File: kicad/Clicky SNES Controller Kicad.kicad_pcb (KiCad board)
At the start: 2 copper layers, 70.2 x 44.8 mm, 0 parts

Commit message: Set up OSH Park design rules
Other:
- net class Default: clearance 0.2 -> 0.1524; trace_width 0.25 -> 0.1524; via_dia 0.6 -> 0.6858; via_drill 0.4 -> 0.3302
- rule trace_clearance: 0.2 -> 0.1524
- rule trace_min: 0.2 -> 0.1524
- rule via_min_drill: 0.3 -> 0.3302
- rule via_min_size: 0.4 -> 0.6858
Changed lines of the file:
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@@
     (links 0)
     (no_connects 0)
-    (area 13.71421 14.16482 172.72886 59.104601)
-    (thickness 1.6)
+    (area 13.71421 14.16482 181.453135 62.567801)
+    (thickness 1.6002)
     (drawings 175)
     (tracks 0)
@@
     (0 F.Cu signal)
     (31 B.Cu signal)
-    (32 B.Adhes user)
-    (33 F.Adhes user)
-    (34 B.Paste user)
-    (35 F.Paste user)
+    (32 B.Adhes user hide)
+    (33 F.Adhes user hide)
+    (34 B.Paste user hide)
+    (35 F.Paste user hide)
     (36 B.SilkS user)
     (37 F.SilkS user)
@@
     (40 Dwgs.User user)
     (41 Cmts.User user)
-    (42 Eco1.User user)
-    (43 Eco2.User user)
+    (42 Eco1.User user hide)
+    (43 Eco2.User user hide)
     (44 Edge.Cuts user)
-    (45 Margin user)
-    (46 B.CrtYd user)
-    (47 F.CrtYd user)
-    (48 B.Fab user)
-    (49 F.Fab user)
+    (45 Margin user hide)
+    (46 B.CrtYd user hide)
+    (47 F.CrtYd user hide)
+    (48 B.Fab user hide)
+    (49 F.Fab user hide)
   )
   (setup
-    (last_trace_width 0.25)
-    (trace_clearance 0.2)
+    (last_trace_width 0.1524)
+    (trace_clearance 0.1524)
     (zone_clearance 0.508)
     (zone_45_only no)
-    (trace_min 0.2)
+    (trace_min 0.1524)
     (segment_width 0.2)
     (edge_width 0.15)
-    (via_size 0.6)
-    (via_drill 0.4)
-    (via_min_size 0.4)
-    (via_min_drill 0.3)
-    (uvia_size 0.3)
-    (uvia_drill 0.1)
+    (via_size 0.6858)
+    (via_drill 0.3302)
+    (via_min_size 0.6858)
+    (via_min_drill 0.3302)
+    (uvia_size 0.762)
+    (uvia_drill 0.508)
     (uvias_allowed no)
-    (uvia_min_size 0.2)
-    (uvia_min_drill 0.1)
+    (uvia_min_size 0.762)
+    (uvia_min_drill 0.508)
     (pcb_text_width 0.3)
     (pcb_text_size 1.5 1.5)
@@
   (net 0 "")
   (net_class Default "This is the default net class."
-    (clearance 0.2)
-    (trace_width 0.25)
-    (via_dia 0.6)
-    (via_drill 0.4)
-    (uvia_dia 0.3)
-    (uvia_drill 0.1)
+    (clearance 0.1524)
+    (trace_width 0.1524)
+    (via_dia 0.6858)
+    (via_drill 0.3302)
+    (uvia_dia 0.762)
+    (uvia_drill 0.508)
   )
   (dimension 9.118742 (width 0.3) (layer Cmts.User)

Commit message: Restart PCB with OSH Park blank template
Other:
- board outline removed
- net class 0.2mm added: clearance 0.2, trace_width 0.2, via_dia 0.6858, via_drill 0.3302
- net class Default: clearance 0.1524 -> 0.254; trace_width 0.1524 -> 0.254
- net class Minimal added: clearance 0.1524, trace_width 0.1524, via_dia 0.6858, via_drill 0.3302
- rule pad_to_mask_clearance: 0.2 -> 0.05
- rule trace_clearance: 0.1524 -> 0.254

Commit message: PCB Rev 2: Create basic board outline
Re-imported the vector drawing of the mechanical board outline and put
the mirrored copy on a different layer so it can be differentiated by
color.
Eco1.User is the unmirrored drawing.
Eco2.User is the mirrored drawing

Added some mechanical keep-out areas to these layers as well.
I probably need two new layers for these but, for now, they are on the
same user layers.
The wide circles on Eco1.User are the keep-out areas behind the d-pad;
so these will actually collide with components placed on the back side
of the board.
The wide circles on Eco2.User are the keep-out areas behind the ABXY
buttons; so these will actually collide with components placed on the
front side of the board.

Created a board outline only for the main section.
I think I will need the extra room and have to use all 3 of these
for the main circuit board. The LR button boards can be done separately
if desired; but, for now, there isn't a good place to stick them
without increasing board rectangular size substantially.
Also OSH Park doesn't support V-grooves.
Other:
- board outline added: 41.9 x 44.8 mm

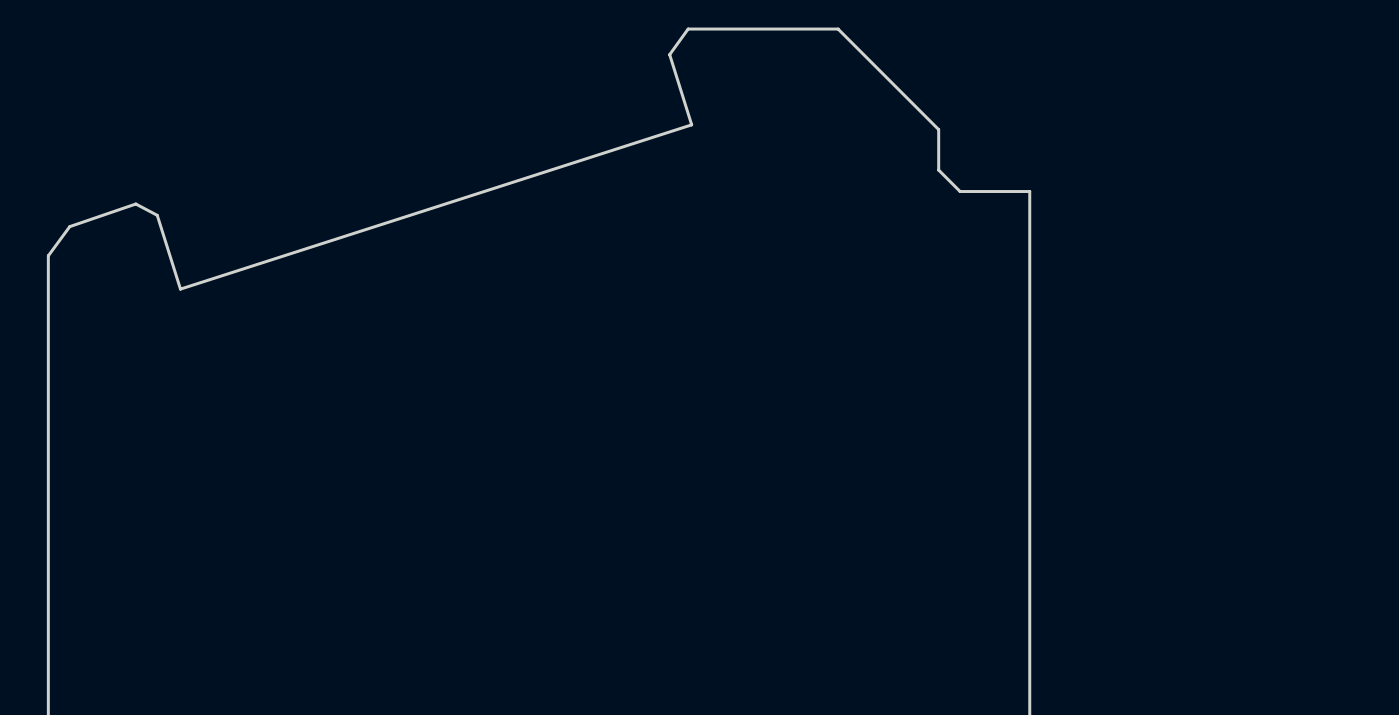
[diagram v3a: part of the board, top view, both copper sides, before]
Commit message: PCB Rev 2: Add mounting holes
Added some drill holes to the main board.
Still need to figure out the final position for the hole on the start /
select board, but a placeholder is in the file for now.
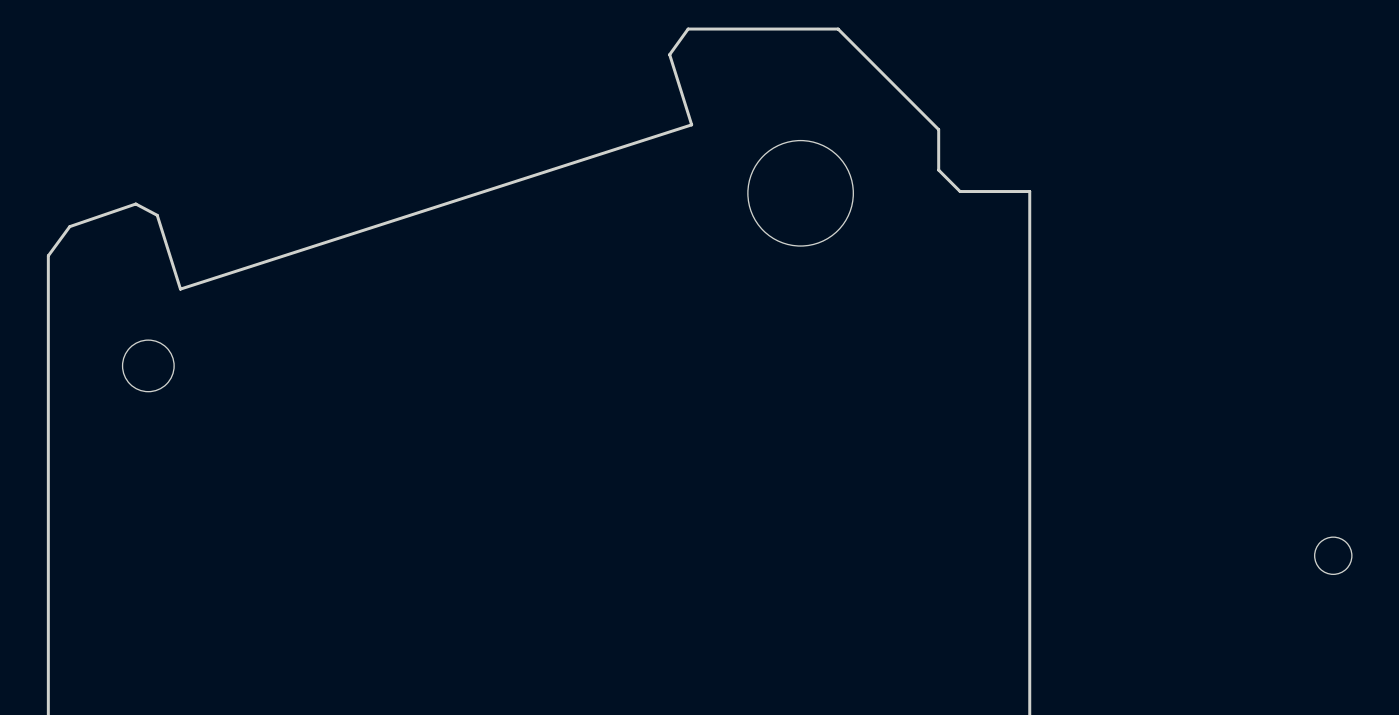
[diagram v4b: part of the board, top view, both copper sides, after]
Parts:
- added REF**: MountingHole_2.2mm_M2, Mounting_Holes:MountingHole_2.2mm_M2, F.Cu at (17.0, 27.4)
- added REF**: MountingHole_4.5mm, Mounting_Holes:MountingHole_4.5mm, F.Cu at (44.8, 20.0)
- added REF**: MountingHole_1_16th, Mounting_Holes:MountingHole_2.2mm_M2, F.Cu at (67.6, 35.5)
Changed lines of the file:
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@@
     (area 12.64741 12.76782 186.348413 57.779876)
     (thickness 1.6)
-    (drawings 174)
+    (drawings 177)
     (tracks 0)
     (zones 0)
-    (modules 0)
+    (modules 3)
     (nets 1)
   )
@@
     (mod_text_size 0.6 0.6)
     (mod_text_width 0.127)
-    (pad_size 1.524 1.524)
-    (pad_drill 0.762)
+    (pad_size 1.5875 1.5875)
+    (pad_drill 1.5875)
     (pad_to_mask_clearance 0.05)
     (pad_to_paste_clearance -0.04)
     (aux_axis_origin 0 0)
-    (visible_elements 7FFFFFFF)
+    (visible_elements 7FFFFF7F)
     (pcbplotparams
       (layerselection 0x3ffff_80000001)
@@
     (uvia_drill 0.127)
   )
+  (module Mounting_Holes:MountingHole_2.2mm_M2 (layer F.Cu)
+    (at 16.9926 27.3558)
+    (descr "Mounting Hole 2.2mm, no annular, M2")
+    (tags "mounting hole 2.2mm no annular m2")
+    (fp_text reference REF** (at 0 -3.2) (layer F.SilkS) hide
+      (effects (font (size 1 1) (thickness 0.15)))
+    )
+    (fp_text value MountingHole_2.2mm_M2 (at 0 3.2) (layer F.Fab) hide
+      (effects (font (size 1 1) (thickness 0.15)))
+    )
+    (fp_circle (center 0 0) (end 2.2 0) (layer Cmts.User) (width 0.15))
+    (fp_circle (center 0 0) (end 2.45 0) (layer F.CrtYd) (width 0.05))
+    (pad 1 np_thru_hole circle (at 0 0) (size 2.2 2.2) (drill 2.2) (layers *.Cu *.Mask))
+  )
+  (module Mounting_Holes:MountingHole_4.5mm (layer F.Cu)
+    (at 44.831 19.9898)
+    (descr "Mounting Hole 4.5mm, no annular")
+    (tags "mounting hole 4.5mm no annular")
+    (fp_text reference REF** (at 0 -5.5) (layer F.SilkS) hide
+      (effects (font (size 1 1) (thickness 0.15)))
+    )
+    (fp_text value MountingHole_4.5mm (at 0 5.5) (layer F.Fab) hide
+      (effects (font (size 1 1) (thickness 0.15)))
+    )
+    (fp_circle (center 0 0) (end 4.5 0) (layer Cmts.User) (width 0.15))
+    (fp_circle (center 0 0) (end 4.75 0) (layer F.CrtYd) (width 0.05))
+    (pad 1 np_thru_hole circle (at 0 0) (size 4.5 4.5) (drill 4.5) (layers *.Cu *.Mask))
+  )
+  (module Mounting_Holes:MountingHole_2.2mm_M2 (layer F.Cu)
+    (at 67.564 35.4584)
+    (descr "Mounting Hole 2.2mm, no annular, M2")
+    (tags "mounting hole 2.2mm no annular m2")
+    (fp_text reference REF** (at 0 -3.2) (layer F.SilkS) hide
+      (effects (font (size 1 1) (thickness 0.15)))
+    )
+    (fp_text value MountingHole_1_16th (at 0 3.2) (layer F.Fab) hide
+      (effects (font (size 1 1) (thickness 0.15)))
+    )
+    (fp_circle (center 0 0) (end 2.2 0) (layer Cmts.User) (width 0.15))
+    (fp_circle (center 0 0) (end 2.45 0) (layer F.CrtYd) (width 0.05))
+    (pad "" np_thru_hole circle (at 0 0) (size 1.5875 1.5875) (drill 1.5875) (layers *.Cu *.Mask))
+  )
+  (gr_circle (center 67.564 35.4584) (end 69.99605 35.4584) (layer B.CrtYd) (width 1.143))
+  (gr_circle (center 44.831 19.9898) (end 47.752 19.9898) (layer B.CrtYd) (width 1.143))
+  (gr_circle (center 16.9926 27.3558) (end 19.2532 27.3558) (layer F.CrtYd) (width 1.143))
   (gr_circle (center 34.8488 37.7698) (end 40.259 37.7698) (layer Eco2.User) (width 1.143))
   (gr_circle (center 34.8488 37.7698) (end 46.75505 37.7698) (layer Eco2.User) (width 1.143))

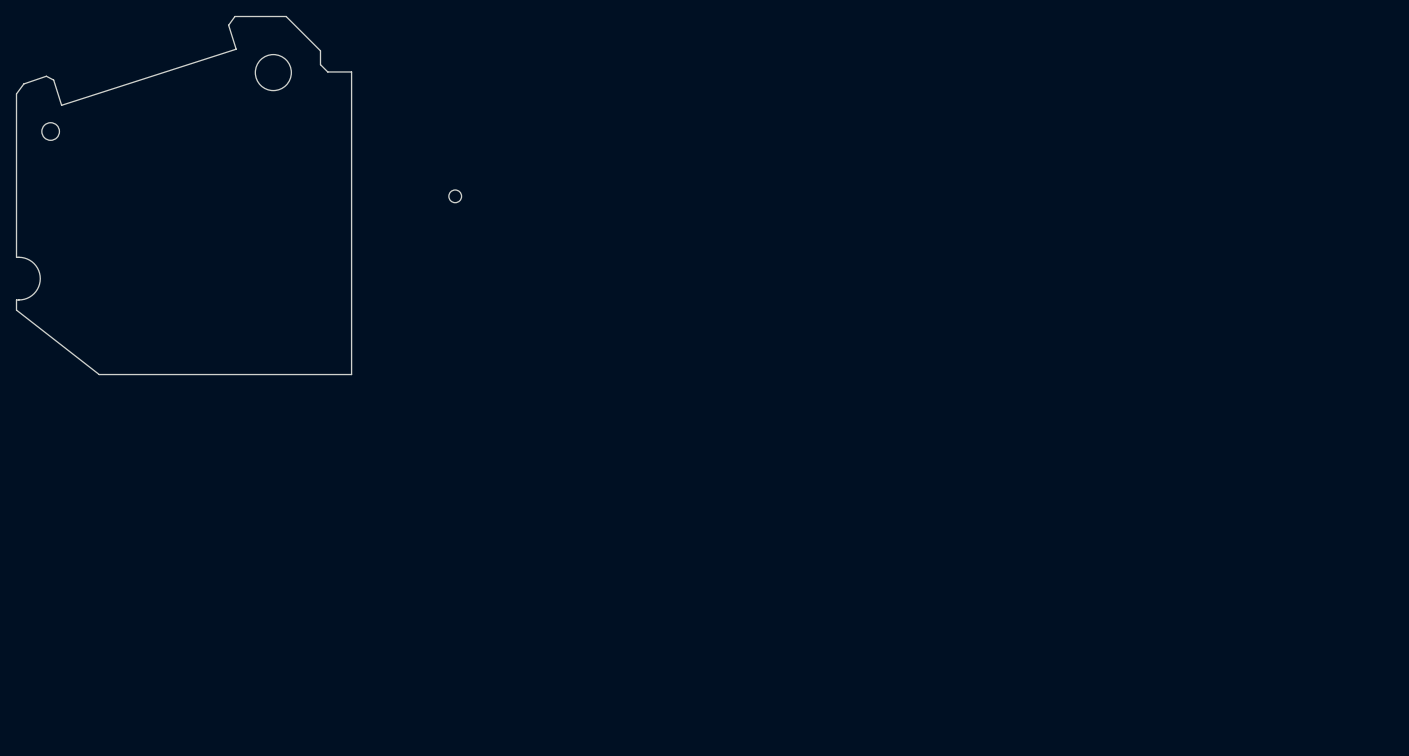
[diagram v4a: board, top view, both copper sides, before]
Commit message: PCB: Import netlist and arrange large components
This is a first pass at laying out the components.
There is definitely a problem with the netlist, though.
Many of the connectors are showing that they only have 1 pin instead of
2 or 3.
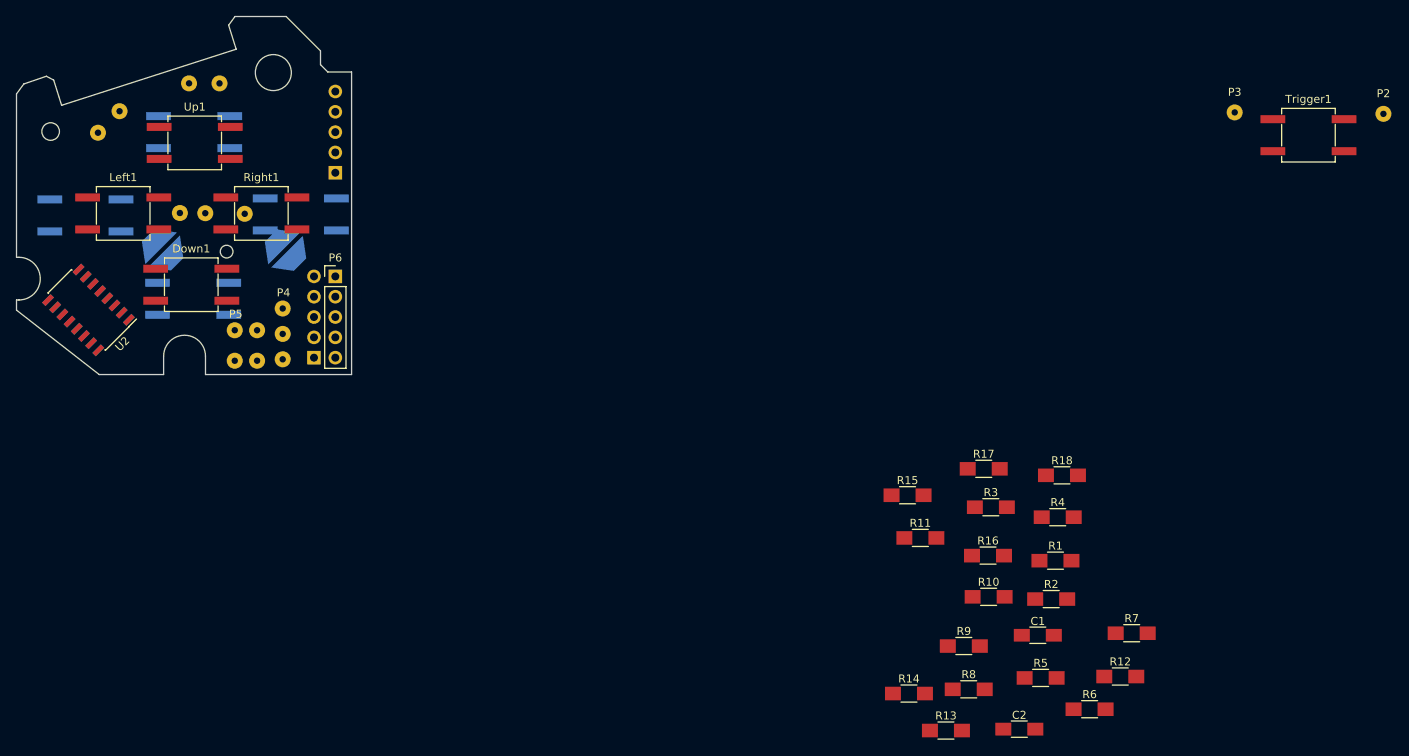
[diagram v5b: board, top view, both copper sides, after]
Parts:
- added A1: SW_PUSH, Extra_Buttons_Switches_SMD:SW_SPST_KSC7-G, B.Cu at (21.3, 37.8)
- added B1: SW_PUSH, Extra_Buttons_Switches_SMD:SW_SPST_KSC7-G, B.Cu at (34.8, 48.3)
- added C1: .1u, Capacitors_SMD:C_1206_HandSoldering, F.Cu at (140.4, 90.3)
- added C2: .1u, Capacitors_SMD:C_1206_HandSoldering, F.Cu at (138.1, 102.1)
- added Down1: SW_PUSH, Extra_Buttons_Switches_SMD:SW_SPST_KSC2-G, F.Cu at (34.6, 46.5)
- added Left1: SW_PUSH, Extra_Buttons_Switches_SMD:SW_SPST_KSC2-G, F.Cu at (26.1, 37.6)
- added P1: CN1, Pin_Headers:Pin_Header_Angled_1x05_Pitch2.54mm, B.Cu at (52.6, 32.5)
- added P10: SHIFT_PORT_ABXY, Pin_Headers:Pin_Header_Straight_1x05_Pitch2.54mm, B.Cu at (49.9, 55.6)
- added P11: TL_LINK_ABXY, Wire_Pads:SolderWirePad_2x_0-8mmDrill, B.Cu at (36.2, 21.3)
- added P12: YB_LINK_ABXY, Wire_Pads:SolderWirePad_2x_0-8mmDrill, B.Cu at (42.8, 54.1)
- added P13: TR_LINK_ABXY, Wire_Pads:SolderWirePad_2x_0-8mmDrill, B.Cu at (24.3, 26.2)
- added P2: VSS_LINK_Trigger, Wire_Pads:SolderWirePad_single_0-8mmDrill, F.Cu at (183.6, 25.1)
- added P3: TR_TL_LINK_Trigger, Wire_Pads:SolderWirePad_single_0-8mmDrill, F.Cu at (165.0, 25.0)
- added P4: SelStart_LINK_DPAD, Wire_Pads:SolderWirePad_3x_0-8mmDrill, F.Cu at (46.0, 52.7)
- added P5: YB_LINK_DPAD, Wire_Pads:SolderWirePad_2x_0-8mmDrill, F.Cu at (40.0, 54.1)
- added P6: SHIFT_PORT_DPAD, Pin_Headers:Pin_Header_Straight_1x05_Pitch2.54mm, F.Cu at (52.6, 45.5)
- added P7: VSS_LINK_SelStart, Wire_Pads:SolderWirePad_single_0-8mmDrill, B.Cu at (36.3, 37.6)
- added P8: Select_LINK_SelStart, Wire_Pads:SolderWirePad_single_0-8mmDrill, B.Cu at (41.2, 37.6)
- added P9: Start_LINK_SelStart, Wire_Pads:SolderWirePad_single_0-8mmDrill, B.Cu at (33.1, 37.5)
- added R1: 47k, Resistors_SMD:R_1206_HandSoldering, F.Cu at (142.6, 81.0)
- added R10: 47k, Resistors_SMD:R_1206_HandSoldering, F.Cu at (134.2, 85.5)
- added R11: 47k, Resistors_SMD:R_1206_HandSoldering, F.Cu at (125.7, 78.2)
- added R12: 47k, Resistors_SMD:R_1206_HandSoldering, F.Cu at (150.7, 95.5)
- added R13: 47k, Resistors_SMD:R_1206_HandSoldering, F.Cu at (128.9, 102.2)
- added R14: 47k, Resistors_SMD:R_1206_HandSoldering, F.Cu at (124.3, 97.6)
- added R15: 47k, Resistors_SMD:R_1206_HandSoldering, F.Cu at (124.1, 72.8)
- added R16: 47k, Resistors_SMD:R_1206_HandSoldering, F.Cu at (134.2, 80.4)
- added R17: 47k, Resistors_SMD:R_1206_HandSoldering, F.Cu at (133.6, 69.5)
- added R18: 47k, Resistors_SMD:R_1206_HandSoldering, F.Cu at (143.4, 70.3)
- added R2: 47k, Resistors_SMD:R_1206_HandSoldering, F.Cu at (142.1, 85.8)
- added R3: 47k, Resistors_SMD:R_1206_HandSoldering, F.Cu at (134.5, 74.3)
- added R4: 47k, Resistors_SMD:R_1206_HandSoldering, F.Cu at (142.9, 75.6)
- added R5: 47k, Resistors_SMD:R_1206_HandSoldering, F.Cu at (140.7, 95.7)
- added R6: 47k, Resistors_SMD:R_1206_HandSoldering, F.Cu at (146.9, 99.6)
- added R7: 47k, Resistors_SMD:R_1206_HandSoldering, F.Cu at (152.1, 90.1)
- added R8: 47k, Resistors_SMD:R_1206_HandSoldering, F.Cu at (131.7, 97.1)
- added R9: 47k, Resistors_SMD:R_1206_HandSoldering, F.Cu at (131.1, 91.7)
- added Right1: SW_PUSH, Extra_Buttons_Switches_SMD:SW_SPST_KSC2-G, F.Cu at (43.3, 37.6)
- added Select1: SW_PUSH, Extra_Buttons_Switches_SMD:SW_SPST_Plated_Pad_5.5mm, B.Cu at (46.4, 42.2)
- added Start1: SW_PUSH, Extra_Buttons_Switches_SMD:SW_SPST_Plated_Pad_5.5mm, B.Cu at (31.0, 42.1)
- added Trigger1: SW_PUSH, Extra_Buttons_Switches_SMD:SW_SPST_KSC6-G, F.Cu at (174.2, 27.8)
- added U1: 4021_DPAD, Housings_SOIC:SOIC-16_3.9x9.9mm_Pitch1.27mm, B.Cu at (21.7, 49.7)
- added U2: 4021_ABXY, Housings_SOIC:SOIC-16_3.9x9.9mm_Pitch1.27mm, F.Cu at (21.7, 49.7)
- added Up1: SW_PUSH, Extra_Buttons_Switches_SMD:SW_SPST_KSC2-G, F.Cu at (35.0, 28.8)
- added X1: SW_PUSH, Extra_Buttons_Switches_SMD:SW_SPST_KSC7-G, B.Cu at (34.9, 27.4)
- added Y1: SW_PUSH, Extra_Buttons_Switches_SMD:SW_SPST_KSC7-G, B.Cu at (48.3, 37.7)
- moved REF** 29.4 mm to (39.0, 42.4)
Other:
- outline, holes or cut-outs redrawn
